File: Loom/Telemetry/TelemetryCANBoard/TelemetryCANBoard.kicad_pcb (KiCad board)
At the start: 2 copper layers, 69.8 x 35.6 mm, 16 parts, among them J1 Conn_01x06, J2 Conn_01x06, J3 Conn_01x02, U1 MCP2551-I-P, U2 MCP2515-xSO, Y1 16M

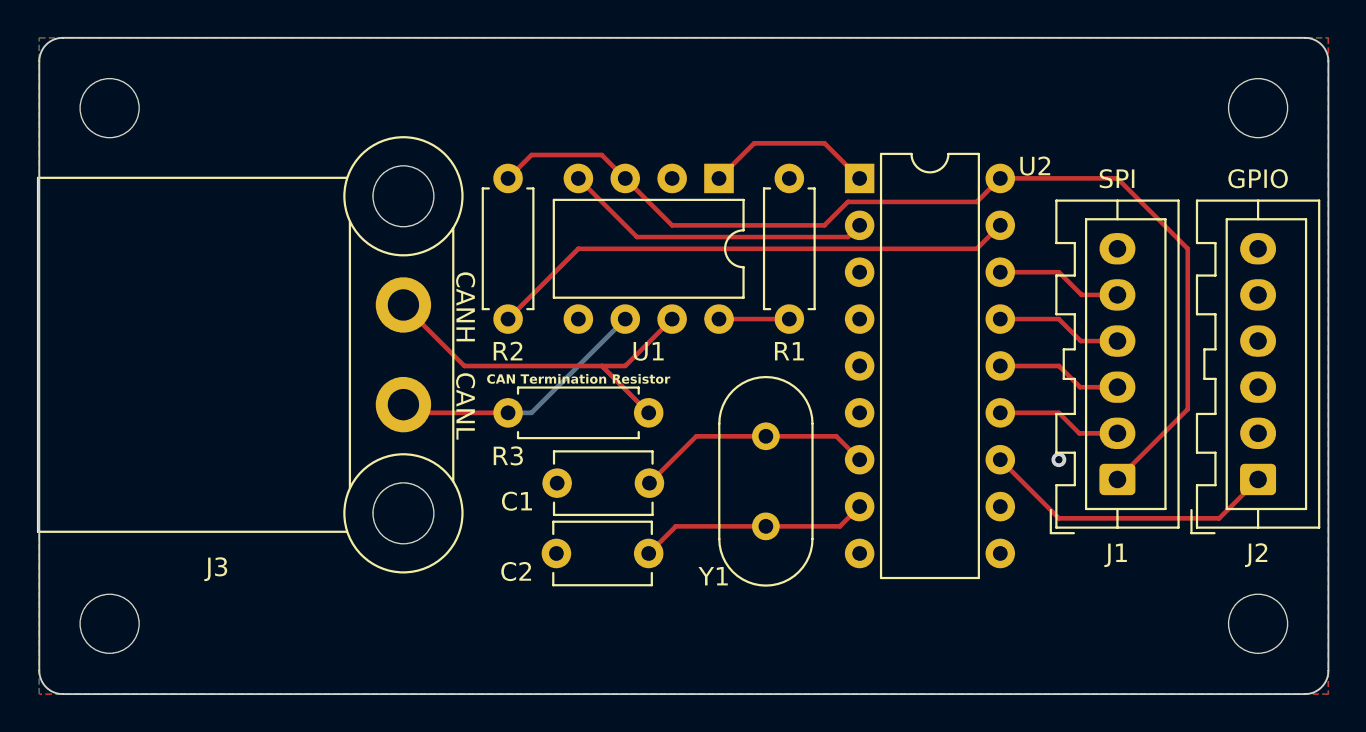
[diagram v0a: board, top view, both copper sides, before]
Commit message: Minor layout and silkscreen changes
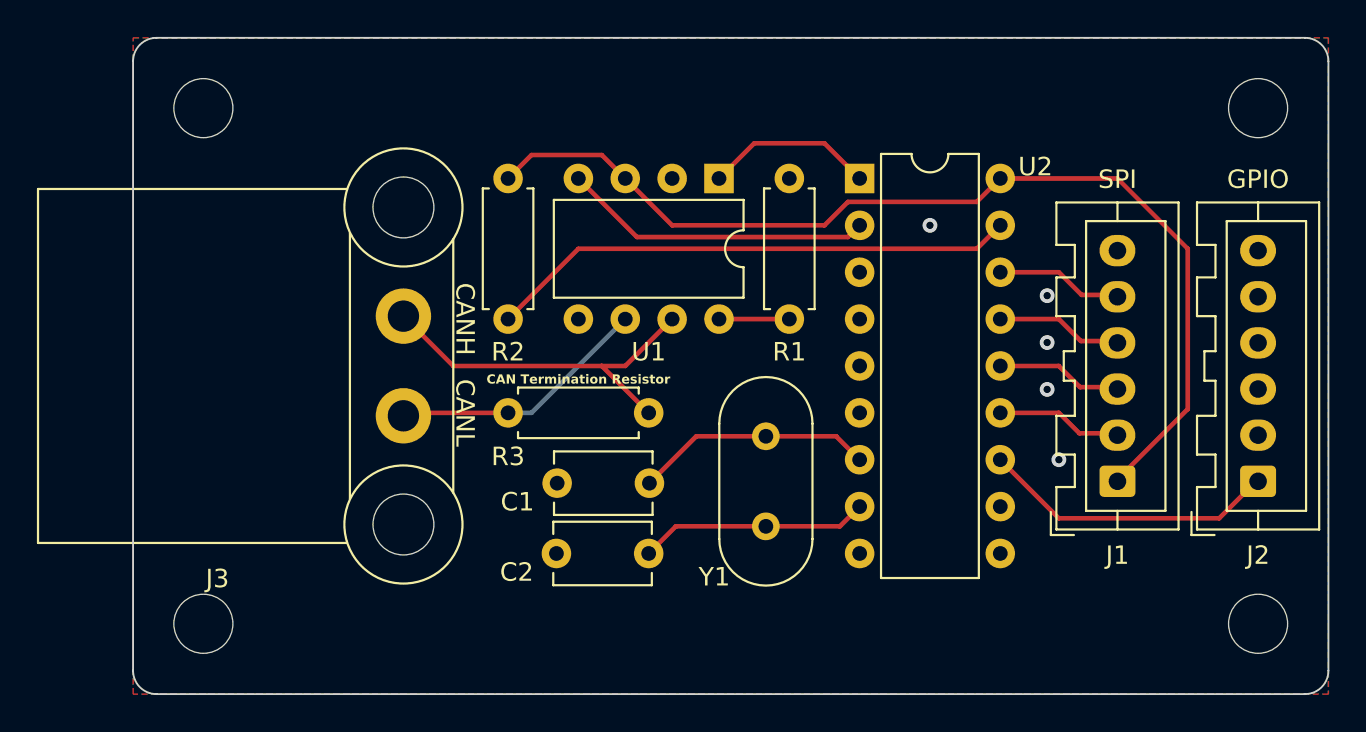
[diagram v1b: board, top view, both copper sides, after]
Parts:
- moved G*** 5.59 mm to (127.5, 92.5)
- moved MNT3 5.08 mm to (128.3, 78.7)
- moved MNT4 5.08 mm to (128.3, 106.7)
- moved J3 0.61 mm to (139.1, 90.0)
- moved J1 0.10 mm to (177.8, 99.0)
- moved J2 0.10 mm to (185.4, 99.0)
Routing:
- net /CANL: track 14.3 -> 14.8 mm
- net GND: vias 1 -> 5
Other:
- board size 69.8 x 35.6 mm -> 64.8 x 35.6 mm
- board text added: "+5V"
- board text added: "CS"
- board text added: "GND"
- board text added: "INT"
- board text added: "MISO"
- board text added: "MOSI"
- board text added: "NC"
- board text added: "SCK"
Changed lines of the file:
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@@
   (net 25 "unconnected-(U2-~{RX0BF}-Pad11)")
   (footprint "MountingHole:MountingHole_3.2mm_M3" (layer "F.Cu")
-    (at 123.19 106.68)
+    (at 128.27 106.68)
     (descr "Mounting Hole 3.2mm, no annular, M3")
     (tags "mounting hole 3.2mm no annular m3")
@@
   )
   (footprint "Connector_JST:JST_XA_B06B-XASK-1_1x06_P2.50mm_Vertical" (layer "F.Cu")
-    (at 177.8 98.86 90)
+    (at 177.8 98.96 90)
     (descr "JST XA series connector, B06B-XASK-1 (http://www.jst-mfg.com/product/pdf/eng/eXA1.pdf), generated with kicad-footprint-generator")
     (tags "connector JST XA vertical")
@@
   )
   (footprint "CAN PCB Footprints:ATF13-2P-BM03" (layer "F.Cu")
-    (at 139.11 89.405 -90)
+    (at 139.11 90.01 -90)
     (property "Sheetfile" "TelemetryCANBoard.kicad_sch")
     (property "Sheetname" "")
@@
   )
   (footprint "Connector_JST:JST_XA_B06B-XASK-1_1x06_P2.50mm_Vertical" (layer "F.Cu")
-    (at 185.42 98.86 90)
+    (at 185.42 98.96 90)
     (descr "JST XA series connector, B06B-XASK-1 (http://www.jst-mfg.com/product/pdf/eng/eXA1.pdf), generated with kicad-footprint-generator")
     (tags "connector JST XA vertical")
@@
   )
   (footprint "MountingHole:MountingHole_3.2mm_M3" (layer "F.Cu")
-    (at 123.19 78.74)
+    (at 128.27 78.74)
     (descr "Mounting Hole 3.2mm, no annular, M3")
     (tags "mounting hole 3.2mm no annular m3")
@@
   )
   (footprint "Additional Footprints:FBR_logo_for_PCB" (layer "B.Cu")
-    (at 121.92 92.456 -90)
+    (at 127.508 92.456 -90)
     (attr through_hole board_only exclude_from_pos_files exclude_from_bom)
     (fp_text reference "G***" (at 0 0 90) (layer "B.SilkS") hide
@@
       (stroke (width 0.01) (type solid)) (fill solid) (layer "B.SilkS"))
   )
-  (gr_line (start 187.96 74.93) (end 120.65 74.93)
+  (gr_line (start 187.96 74.93) (end 125.73 74.93)
     (stroke (width 0.1) (type default)) (layer "Edge.Cuts"))
   (gr_line (start 189.23 109.22) (end 189.23 76.2)
     (stroke (width 0.1) (type default)) (layer "Edge.Cuts"))
-  (gr_line (start 119.38 76.2) (end 119.38 109.22)
+  (gr_line (start 124.46 76.2) (end 124.46 109.22)
     (stroke (width 0.1) (type default)) (layer "Edge.Cuts"))
-  (gr_line (start 187.96 110.49) (end 120.65 110.49)
+  (gr_line (start 187.96 110.49) (end 125.73 110.49)
     (stroke (width 0.1) (type default)) (layer "Edge.Cuts"))
   (gr_arc (start 189.23 109.22) (mid 188.858026 110.118026) (end 187.96 110.49)
     (stroke (width 0.1) (type default)) (layer "Edge.Cuts"))
-  (gr_arc (start 119.38 76.2) (mid 119.751974 75.301974) (end 120.65 74.93)
+  (gr_arc (start 124.46 76.2) (mid 124.831974 75.301974) (end 125.73 74.93)
     (stroke (width 0.1) (type default)) (layer "Edge.Cuts"))
   (gr_arc (start 187.96 74.93) (mid 188.858026 75.301974) (end 189.23 76.2)
     (stroke (width 0.1) (type default)) (layer "Edge.Cuts"))
-  (gr_arc (start 120.65 110.49) (mid 119.751974 110.118026) (end 119.38 109.22)
+  (gr_arc (start 125.73 110.49) (mid 124.831974 110.118026) (end 124.46 109.22)
     (stroke (width 0.1) (type default)) (layer "Edge.Cuts"))
-  (gr_text "Telemetry CAN to SPI board\nDesigned by Oliver Gaskell" (at 126.492 92.456 90) (layer "B.SilkS")
+  (gr_text "INT" (at 187.96 99.06 90) (layer "B.SilkS")
+    (effects (font (size 0.6 0.6) (thickness 0.1) bold) (justify bottom mirror))
+  )
+  (gr_text "GND" (at 180.34 86.36 90) (layer "B.SilkS")
+    (effects (font (size 0.6 0.6) (thickness 0.1) bold) (justify bottom mirror))
+  )
+  (gr_text "GND" (at 187.96 86.36 90) (layer "B.SilkS")
+    (effects (font (size 0.6 0.6) (thickness 0.1) bold) (justify bottom mirror))
+  )
+  (gr_text "NC" (at 187.96 96.52 90) (layer "B.SilkS")
+    (effects (font (size 0.6 0.6) (thickness 0.1) bold) (justify bottom mirror))
+  )
+  (gr_text "NC" (at 187.96 93.98 90) (layer "B.SilkS")
+    (effects (font (size 0.6 0.6) (thickness 0.1) bold) (justify bottom mirror))
+  )
+  (gr_text "+5V" (at 180.34 99.06 90) (layer "B.SilkS")
+    (effects (font (size 0.6 0.6) (thickness 0.1) bold) (justify bottom mirror))
+  )
+  (gr_text "Telemetry CAN to SPI board\nDesigned by Oliver Gaskell" (at 132.08 92.456 90) (layer "B.SilkS")
     (effects (font (size 1 1) (thickness 0.15)) (justify mirror))
   )
-  (gr_text "CANL" (at 141.859 94.869 270) (layer "F.SilkS")
+  (gr_text "MISO" (at 180.34 91.44 90) (layer "B.SilkS")
+    (effects (font (size 0.6 0.6) (thickness 0.1) bold) (justify bottom mirror))
+  )
+  (gr_text "NC" (at 187.96 91.44 90) (layer "B.SilkS")
+    (effects (font (size 0.6 0.6) (thickness 0.1) bold) (justify bottom mirror))
+  )
+  (gr_text "MOSI" (at 180.34 93.98 90) (layer "B.SilkS")
+    (effects (font (size 0.6 0.6) (thickness 0.1) bold) (justify bottom mirror))
+  )
+  (gr_text "GND" (at 187.96 88.9 90) (layer "B.SilkS")
+    (effects (font (size 0.6 0.6) (thickness 0.1) bold) (justify bottom mirror))
+  )
+  (gr_text "SCK" (at 180.34 96.52 90) (layer "B.SilkS")
+    (effects (font (size 0.6 0.6) (thickness 0.1) bold) (justify bottom mirror))
+  )
+  (gr_text "CS" (at 180.34 88.9 90) (layer "B.SilkS")
+    (effects (font (size 0.6 0.6) (thickness 0.1) bold) (justify bottom mirror))
+  )
+  (gr_text "CANL" (at 141.859 95.25 270) (layer "F.SilkS")
     (effects (font (size 1 1) (thickness 0.15)) (justify bottom))
   )
@@
     (effects (font (size 0.5 0.5) (thickness 0.1) bold) (justify bottom))
   )
-  (gr_text "CANH" (at 141.859 89.535 -90) (layer "F.SilkS")
+  (gr_text "CANH" (at 141.859 90.17 -90) (layer "F.SilkS")
     (effects (font (size 1 1) (thickness 0.15)) (justify bottom))
   )
@@
     (effects (font (size 1 1) (thickness 0.15)) (justify bottom))
   )
+  (via (at 167.64 85.09) (size 0.8) (drill 0.4) (layers "F.Cu" "B.Cu") (free) (net 1))
   (via (at 174.625 97.79) (size 0.8) (drill 0.4) (layers "F.Cu" "B.Cu") (free) (net 1))
+  (via (at 173.99 91.44) (size 0.8) (drill 0.4) (layers "F.Cu" "B.Cu") (free) (net 1))
+  (via (at 173.99 88.9) (size 0.8) (drill 0.4) (layers "F.Cu" "B.Cu") (free) (net 1))
+  (via (at 173.99 93.98) (size 0.8) (drill 0.4) (layers "F.Cu" "B.Cu") (free) (net 1))
   (segment (start 158.75 96.52) (end 154.98 96.52) (width 0.25) (layer "F.Cu") (net 2))
   (segment (start 154.98 96.52) (end 152.44 99.06) (width 0.25) (layer "F.Cu") (net 2))
@@
   (segment (start 171.45 97.79) (end 174.625 100.965) (width 0.25) (layer "F.Cu") (net 9))
   (segment (start 183.315 100.965) (end 185.42 98.86) (width 0.25) (layer "F.Cu") (net 9))
-  (segment (start 142.415 92.71) (end 149.86 92.71) (width 0.25) (layer "F.Cu") (net 13))
+  (segment (start 141.81 92.71) (end 139.11 90.01) (width 0.25) (layer "F.Cu") (net 13))
   (segment (start 149.86 92.71) (end 151.13 92.71) (width 0.25) (layer "F.Cu") (net 13))
   (segment (start 151.13 92.71) (end 153.67 90.17) (width 0.25) (layer "F.Cu") (net 13))
-  (segment (start 139.11 89.405) (end 142.415 92.71) (width 0.25) (layer "F.Cu") (net 13))
+  (segment (start 149.86 92.71) (end 141.81 92.71) (width 0.25) (layer "F.Cu") (net 13))
   (segment (start 149.86 92.71) (end 152.4 95.25) (width 0.25) (layer "F.Cu") (net 13))
+  (segment (start 144.78 95.25) (end 139.27 95.25) (width 0.25) (layer "F.Cu") (net 14))
   (segment (start 139.555 95.25) (end 139.11 94.805) (width 0.25) (layer "F.Cu") (net 14))
-  (segment (start 144.78 95.25) (end 139.555 95.25) (width 0.25) (layer "F.Cu") (net 14))
+  (segment (start 139.27 95.25) (end 139.11 95.41) (width 0.25) (layer "F.Cu") (net 14))
   (segment (start 146.05 95.25) (end 144.78 95.25) (width 0.25) (layer "B.Cu") (net 14))
   (segment (start 151.13 90.17) (end 146.05 95.25) (width 0.25) (layer "B.Cu") (net 14))
@@
     (polygon
       (pts
-        (xy 119.38 74.93)
+        (xy 124.46 74.93)
         (xy 189.23 74.93)
         (xy 189.23 110.49)
-        (xy 119.38 110.49)
+        (xy 124.46 110.49)
       )
     )
